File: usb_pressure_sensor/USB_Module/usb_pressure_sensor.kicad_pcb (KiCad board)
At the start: 2 copper layers, 45 x 26 mm, 25 parts, among them IC1 STM32F042F6P6, IC2 MCP1700, J1 CONN_02x09, J2 MODULE_BRIDGE, P1 SWD_TC, U1 MICRO_USB, U2 SN74LVC1GX04, U3 KSC341J:SWITCH, Y1 Crystal 32.768kHz

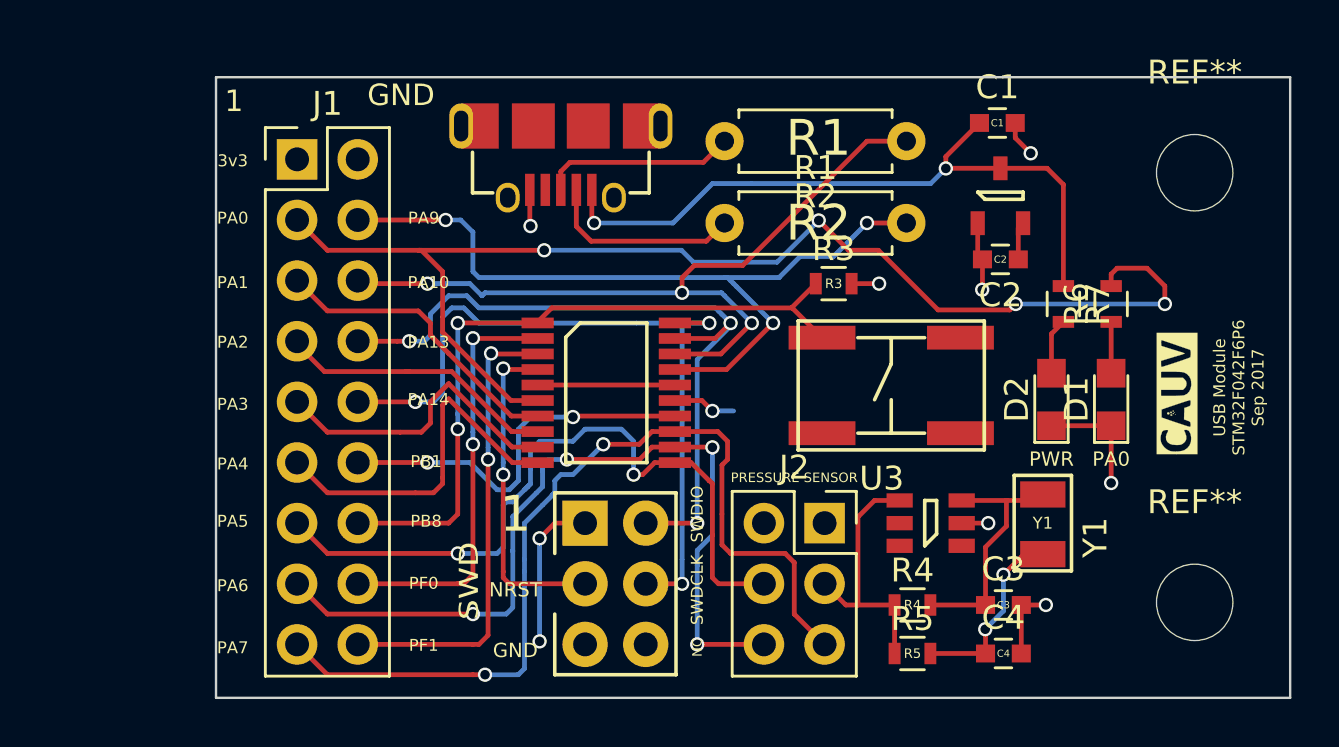
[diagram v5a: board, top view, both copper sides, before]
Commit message: added mounting holes and changed light board footprints
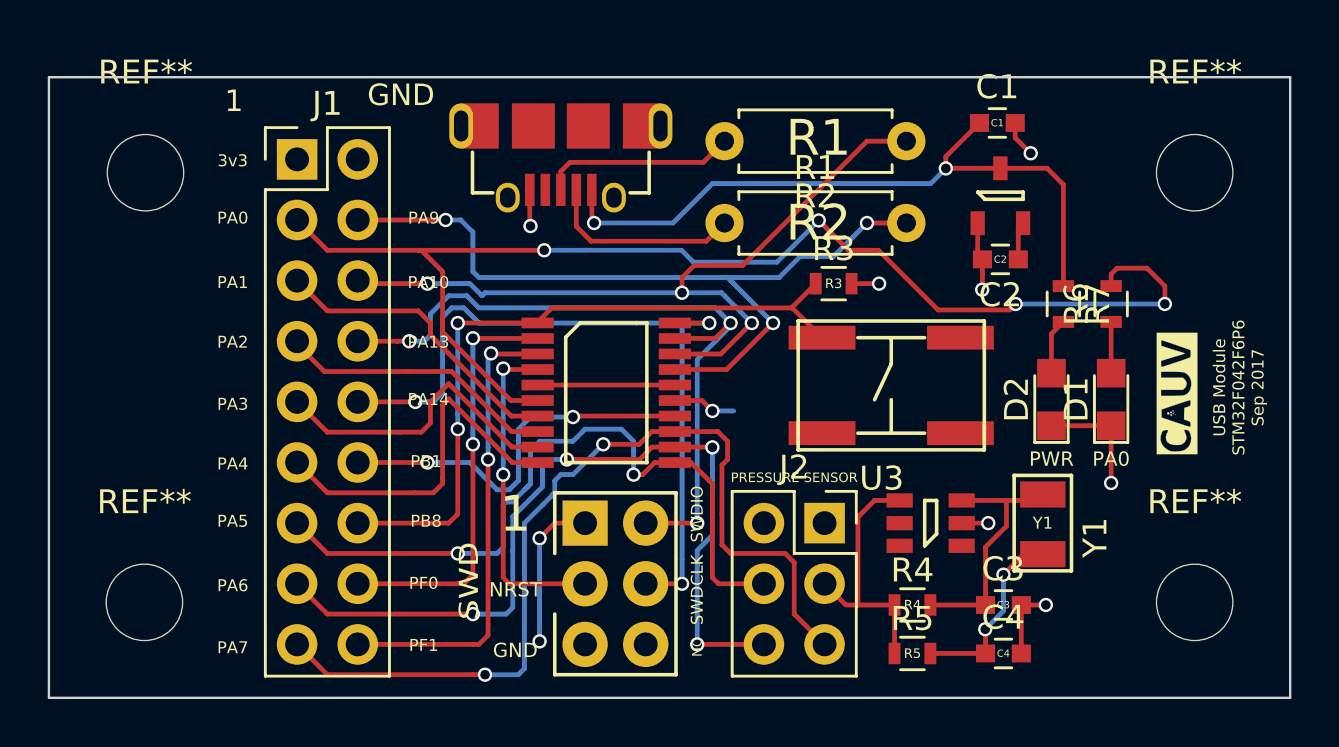
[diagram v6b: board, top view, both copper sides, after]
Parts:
- added REF**: MountingHole_3.2mm_M3, Mounting_Holes:MountingHole_3.2mm_M3, F.Cu at (114.0, 100.0)
- added REF**: MountingHole_3.2mm_M3, Mounting_Holes:MountingHole_3.2mm_M3, F.Cu at (114.0, 118.0)
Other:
- board size 45 x 26 mm -> 52 x 26 mm
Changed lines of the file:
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@@
     (tracks 386)
     (zones 0)
-    (modules 25)
+    (modules 27)
     (nets 33)
   )
   (page A4)
   (layers
-    (0 F.Cu signal hide)
-    (31 B.Cu signal hide)
-    (32 B.Adhes user hide)
-    (33 F.Adhes user hide)
-    (34 B.Paste user hide)
-    (35 F.Paste user hide)
-    (36 B.SilkS user hide)
+    (0 F.Cu signal)
+    (31 B.Cu signal)
+    (32 B.Adhes user)
+    (33 F.Adhes user)
+    (34 B.Paste user)
+    (35 F.Paste user)
+    (36 B.SilkS user)
     (37 F.SilkS user)
-    (38 B.Mask user hide)
-    (39 F.Mask user hide)
-    (40 Dwgs.User user hide)
-    (41 Cmts.User user hide)
-    (42 Eco1.User user hide)
-    (43 Eco2.User user hide)
+    (38 B.Mask user)
+    (39 F.Mask user)
+    (40 Dwgs.User user)
+    (41 Cmts.User user)
+    (42 Eco1.User user)
+    (43 Eco2.User user)
     (44 Edge.Cuts user)
-    (45 Margin user hide)
-    (46 B.CrtYd user hide)
+    (45 Margin user)
+    (46 B.CrtYd user)
     (47 F.CrtYd user)
-    (48 B.Fab user hide)
+    (48 B.Fab user)
     (49 F.Fab user)
   )
@@
     (fp_circle (center 0 0) (end 3.2 0) (layer Cmts.User) (width 0.15))
     (fp_circle (center 0 0) (end 3.45 0) (layer F.CrtYd) (width 0.05))
-    (pad 1 np_thru_hole circle (at 0 0) (size 3.2 3.2) (drill 3.2) (layers *.Cu *.Mask))
+    (pad "" np_thru_hole circle (at 0 0) (size 3.2 3.2) (drill 3.2) (layers *.Cu *.Mask))
   )
   (module Mounting_Holes:MountingHole_3.2mm_M3 (layer F.Cu)
@@
     )
   )
+  (module Mounting_Holes:MountingHole_3.2mm_M3 (layer F.Cu)
+    (at 114.046 100)
+    (descr "Mounting Hole 3.2mm, no annular, M3")
+    (tags "mounting hole 3.2mm no annular m3")
+    (attr virtual)
+    (fp_text reference REF** (at 0 -4.2) (layer F.SilkS)
+      (effects (font (size 1 1) (thickness 0.15)))
+    )
+    (fp_text value MountingHole_3.2mm_M3 (at 0 4.2) (layer F.Fab)
+      (effects (font (size 1 1) (thickness 0.15)))
+    )
+    (fp_text user %R (at 0.3 0) (layer F.Fab)
+      (effects (font (size 1 1) (thickness 0.15)))
+    )
+    (fp_circle (center 0 0) (end 3.2 0) (layer Cmts.User) (width 0.15))
+    (fp_circle (center 0 0) (end 3.45 0) (layer F.CrtYd) (width 0.05))
+    (pad 1 np_thru_hole circle (at 0 0) (size 3.2 3.2) (drill 3.2) (layers *.Cu *.Mask))
+  )
+  (module Mounting_Holes:MountingHole_3.2mm_M3 (layer F.Cu)
+    (at 114 118)
+    (descr "Mounting Hole 3.2mm, no annular, M3")
+    (tags "mounting hole 3.2mm no annular m3")
+    (attr virtual)
+    (fp_text reference REF** (at 0 -4.2) (layer F.SilkS)
+      (effects (font (size 1 1) (thickness 0.15)))
+    )
+    (fp_text value MountingHole_3.2mm_M3 (at 0 4.2) (layer F.Fab)
+      (effects (font (size 1 1) (thickness 0.15)))
+    )
+    (fp_text user %R (at 0.3 0) (layer F.Fab)
+      (effects (font (size 1 1) (thickness 0.15)))
+    )
+    (fp_circle (center 0 0) (end 3.2 0) (layer Cmts.User) (width 0.15))
+    (fp_circle (center 0 0) (end 3.45 0) (layer F.CrtYd) (width 0.05))
+    (pad 1 np_thru_hole circle (at 0 0) (size 3.2 3.2) (drill 3.2) (layers *.Cu *.Mask))
+  )
+  (gr_line (start 110 96) (end 162 96) (layer Edge.Cuts) (width 0.1))
+  (gr_line (start 110 122) (end 110 96) (layer Edge.Cuts) (width 0.1))
+  (gr_line (start 162 122) (end 110 122) (layer Edge.Cuts) (width 0.1))
   (gr_text PA0 (at 154.5 112) (layer F.SilkS)
     (effects (font (size 0.6 0.6) (thickness 0.15)))
@@
     (effects (font (size 0.6 0.6) (thickness 0.15)))
   )
-  (gr_line (start 162 96) (end 117 96) (angle 90) (layer Edge.Cuts) (width 0.1))
   (gr_line (start 162 122) (end 162 96) (angle 90) (layer Edge.Cuts) (width 0.1))
-  (gr_line (start 117 122) (end 162 122) (angle 90) (layer Edge.Cuts) (width 0.1))
-  (gr_line (start 117 96) (end 117 122) (angle 90) (layer Edge.Cuts) (width 0.1))
   (gr_text "USB Module \nSTM32F042F6P6\nSep 2017" (at 159.85 109 90) (layer F.SilkS)
     (effects (font (size 0.5 0.5) (thickness 0.125)))
@@
   (segment (start 152 108.4) (end 152 106.75) (width 0.2) (layer F.Cu) (net 32))
   (segment (start 152 106.75) (end 152.5 106.25) (width 0.2) (layer F.Cu) (net 32))
+  (zone (net 3) (net_name /3v3) (layer F.Cu) (hatch edge 0.508)
+    (connect_pads (clearance 0.254))
+    (min_thickness 0.254)
+    (fill yes (arc_segments 16) (thermal_gap 0.508) (thermal_bridge_width 0.508))
+    (polygon
+      (pts
+        (xy 110 122) (xy 110 96) (xy 162 96) (xy 162 122)
+      )
+    )
+  )
   (zone (net 1) (net_name /GND) (layer B.Cu) (hatch edge 0.508)
     (connect_pads (clearance 0.254))
@@
     (polygon
       (pts
-        (xy 162 96.25) (xy 162 122) (xy 117 122) (xy 117 96) (xy 162 96)
+        (xy 110 122) (xy 110 96) (xy 162 96) (xy 162 122)
       )
     )
-  )
-  (zone (net 3) (net_name /3v3) (layer F.Cu) (hatch edge 0.508)
-    (connect_pads (clearance 0.254))
-    (min_thickness 0.254)
-    (fill yes (arc_segments 16) (thermal_gap 0.508) (thermal_bridge_width 0.508))
-    (polygon
-      (pts
-        (xy 162 122) (xy 117 122) (xy 117 96) (xy 162 96)
-      )
-    )

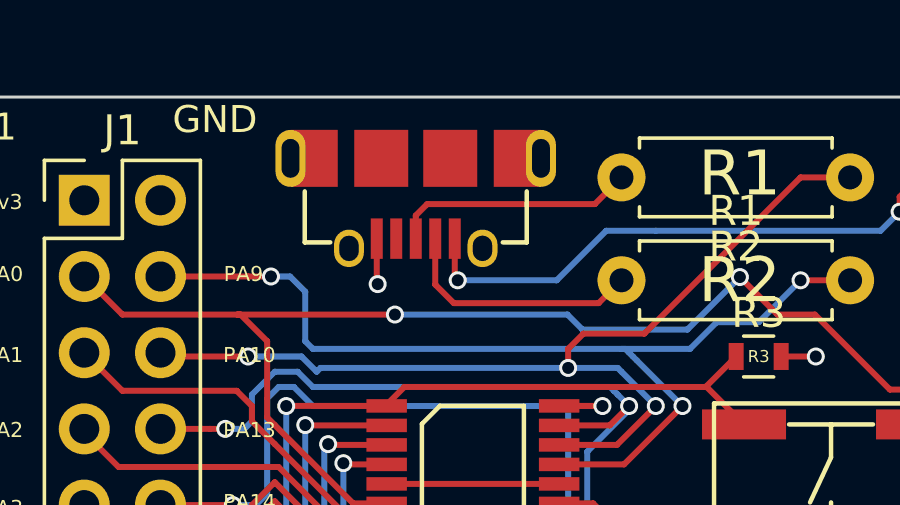
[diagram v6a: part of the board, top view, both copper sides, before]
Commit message: Moved usb connector
Moved connector upwards so that the line on the footprint which represents the pcb edge lines up with the actual pcb edge
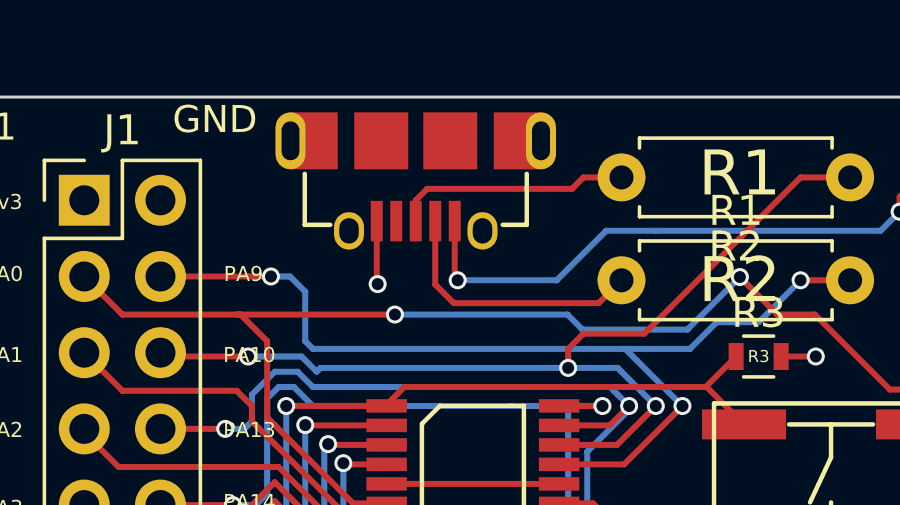
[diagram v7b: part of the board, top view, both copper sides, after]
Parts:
- moved U1 0.58 mm to (131.4, 97.5)
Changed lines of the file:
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@@
-(kicad_pcb (version 4) (host pcbnew 4.0.6)
+(kicad_pcb (version 4) (host pcbnew 4.0.6-e0-6349~53~ubuntu16.04.1)
   (general
     (links 63)
-    (no_connects 0)
-    (area 116.704095 93.319 167.557143 123.275)
+    (no_connects 1)
+    (area 104.442857 93.319 167.557143 123.275)
     (thickness 1.6)
     (drawings 37)
-    (tracks 386)
+    (tracks 388)
     (zones 0)
     (modules 27)
@@
   )
   (module agg:MICROUSB_MOLEX_47589-0001 (layer F.Cu)
-    (at 131.445 98.044 180)
+    (at 131.445 97.4598 180)
     (fp_text reference U1 (at 0 -4.75 180) (layer F.Fab)
       (effects (font (size 1 1) (thickness 0.15)))
@@
   (segment (start 143.383 118.11) (end 143.891 118.11) (width 0.2) (layer F.Cu) (net 23))
   (segment (start 143.891 118.11) (end 145.427 118.11) (width 0.2) (layer F.Cu) (net 23))
+  (segment (start 132.715 102.87) (end 137.541 102.87) (width 0.2) (layer F.Cu) (net 25))
   (segment (start 132.095 100.719) (end 132.095 102.25) (width 0.2) (layer F.Cu) (net 25))
   (segment (start 137.541 102.87) (end 138.303 102.108) (width 0.2) (layer F.Cu) (net 25))
-  (segment (start 132.715 102.87) (end 137.541 102.87) (width 0.2) (layer F.Cu) (net 25))
   (segment (start 132.095 102.25) (end 132.715 102.87) (width 0.2) (layer F.Cu) (net 25))
+  (segment (start 138.303 98.679) (end 137.033 98.679) (width 0.2) (layer F.Cu) (net 26))
+  (segment (start 131.445 99.441) (end 131.445 100.1348) (width 0.2) (layer F.Cu) (net 26))
+  (segment (start 131.826 99.06) (end 131.445 99.441) (width 0.2) (layer F.Cu) (net 26))
+  (segment (start 136.652 99.06) (end 131.826 99.06) (width 0.2) (layer F.Cu) (net 26))
+  (segment (start 137.033 98.679) (end 136.652 99.06) (width 0.2) (layer F.Cu) (net 26))
   (segment (start 131.445 100.719) (end 131.445 99.949) (width 0.2) (layer F.Cu) (net 26))
-  (segment (start 137.414 99.568) (end 138.303 98.679) (width 0.2) (layer F.Cu) (net 26))
-  (segment (start 131.826 99.568) (end 137.414 99.568) (width 0.2) (layer F.Cu) (net 26))
-  (segment (start 131.445 99.949) (end 131.826 99.568) (width 0.2) (layer F.Cu) (net 26))
   (segment (start 154.5 108.4) (end 154.5 106.25) (width 0.2) (layer F.Cu) (net 31))
   (segment (start 152 108.4) (end 152 106.75) (width 0.2) (layer F.Cu) (net 32))
